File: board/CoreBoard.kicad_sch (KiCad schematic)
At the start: 4 parts

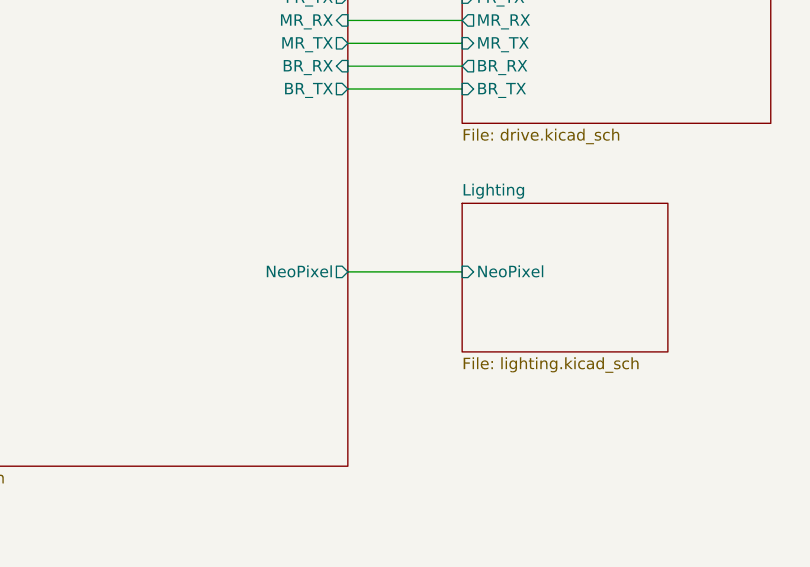
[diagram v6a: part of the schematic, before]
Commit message: routed core board
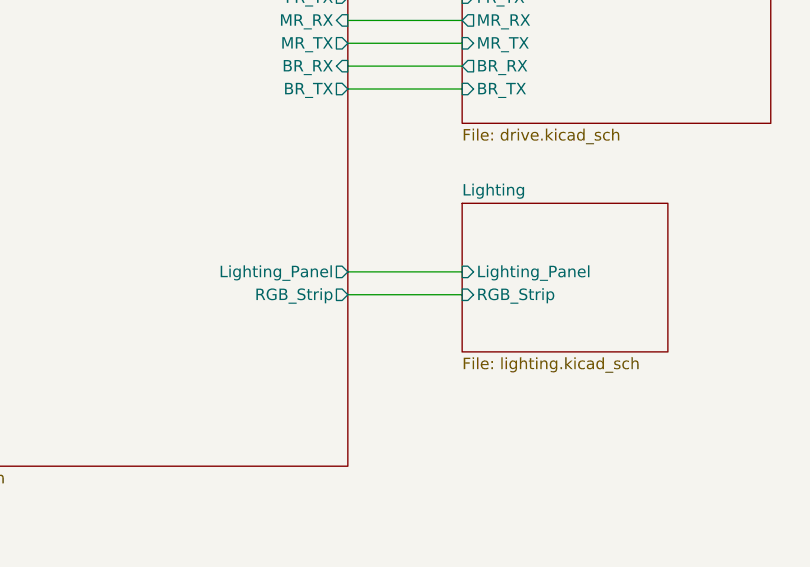
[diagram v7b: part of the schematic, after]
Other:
- sheet Lighting ports: added Lighting_Panel, RGB_Strip; removed NeoPixel
- sheet Teensy ports: added Lighting_Panel, RGB_Strip; removed NeoPixel
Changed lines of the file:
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@@
+	(wire
+		(pts
+			(xy 233.68 181.61) (xy 246.38 181.61)
+		)
+		(stroke
+			(width 0)
+			(type default)
+		)
+	)
 	(wire
 		(pts
@@
 			)
 		)
-		(pin "NeoPixel" output
-			(at 233.68 179.07 0)
-			(effects
-				(font
-					(size 1.27 1.27)
-				)
-				(justify right)
-			)
-		)
 		(pin "SNSR_SCL" output
 			(at 176.53 96.52 180)
@@
 				)
 				(justify left)
+			)
+		)
+		(pin "RGB_Strip" output
+			(at 233.68 181.61 0)
+			(effects
+				(font
+					(size 1.27 1.27)
+				)
+				(justify right)
+			)
+		)
+		(pin "Lighting_Panel" output
+			(at 233.68 179.07 0)
+			(effects
+				(font
+					(size 1.27 1.27)
+				)
+				(justify right)
 			)
 		)
@@
 			)
 		)
-		(pin "NeoPixel" input
+		(pin "Lighting_Panel" input
 			(at 246.38 179.07 180)
 			(effects
 				(font
+					(size 1.27 1.27)
+				)
+				(justify left)
+			)
+		)
+		(pin "RGB_Strip" input
+			(at 246.38 181.61 180)
+			(effects
+				(font

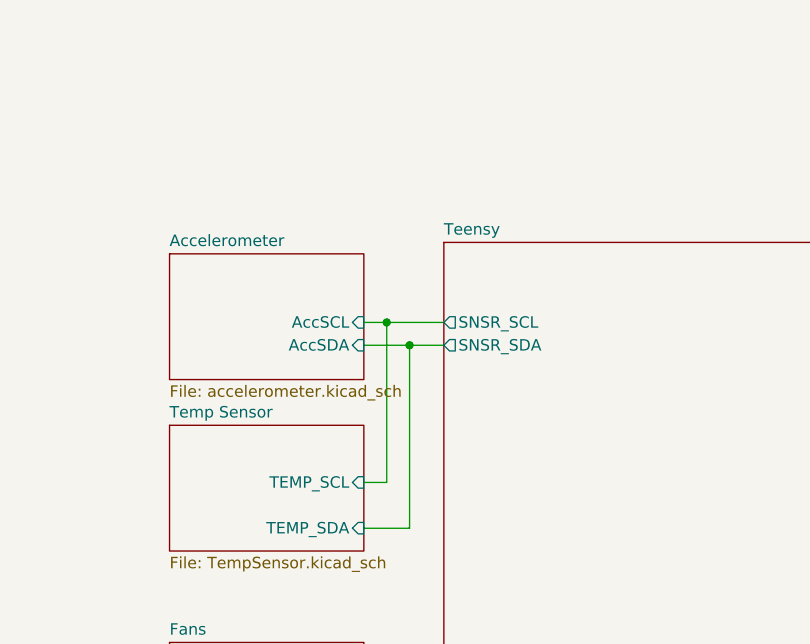
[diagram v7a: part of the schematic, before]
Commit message: Added Silkscreen and Pullup to both schematic and layout
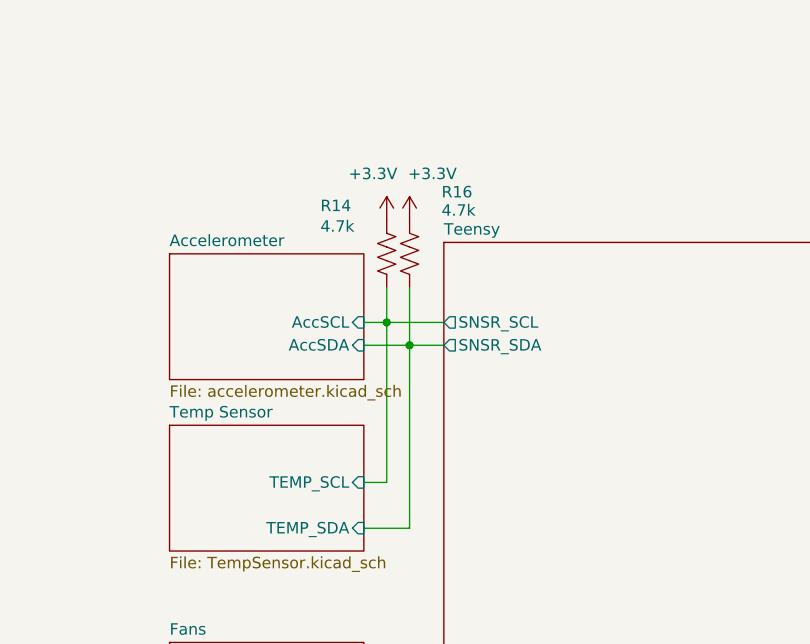
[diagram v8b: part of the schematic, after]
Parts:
- added R14, R16: 4.7k, Resistor_SMD:R_0603_1608Metric_Pad0.98x0.95mm_HandSolder, symbol Device:R_US
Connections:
- net Accelerometer/AccSCL: now also R14.2
- net Accelerometer/AccSDA: now also R16.2
- new net +3.3V: R14.1, R16.1
